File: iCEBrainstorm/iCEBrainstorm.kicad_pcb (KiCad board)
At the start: 2 copper layers, 31 parts, among them J1 Connector, USB-TYPE-C-16P, J2 Conn_01x03_Pin, U1 STM32F103C8T6, U3 ICE40UP5K-SG48ITR, U6 AMS1117, X1 X322516MLB4SI

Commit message: did some things
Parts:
- removed H5: MountingHole_Pad, MountingHole:MountingHole_3.2mm_M3_DIN965_Pad
- removed J2: Conn_01x03_Pin, Connector_PinHeader_2.00mm:PinHeader_1x03_P2.00mm_Vertical
- added C14: 4.7uF, PCM_JLCPCB:C_0805, F.Cu at (67.9, 43.2)
- added C15: 100nF, PCM_JLCPCB:C_0603, F.Cu at (71.1, 47.6)
- added C16: 4.7uF, PCM_JLCPCB:C_0805, F.Cu at (63.8, 50.4)
- added C17: 100nF, PCM_JLCPCB:C_0603, F.Cu at (67.9, 49.2)
- added C18: 4.7uF, PCM_JLCPCB:C_0805, F.Cu at (63.8, 53.5)
- added C19: 100nF, PCM_JLCPCB:C_0603, F.Cu at (67.9, 51.5)
- added C20: 22uF, PCM_JLCPCB:C_0805, F.Cu at (86.4, 72.4)
- added C21: 22uF, PCM_JLCPCB:C_0805, F.Cu at (80.0, 77.5)
- added H4: MountingHole_Pad, MountingHole:MountingHole_2.7mm_Pad, F.Cu at (39.3, 66.1)
- added J3: Conn_01x04_Pin, Connector_PinHeader_2.00mm:PinHeader_1x04_P2.00mm_Vertical, F.Cu at (103.3, 91.4)
- added R4: 5.1kΩ, PCM_JLCPCB:R_0603, F.Cu at (206.2, 75.0)
- added R5: 5.1kΩ, PCM_JLCPCB:R_0603, F.Cu at (206.2, 77.3)
- added R6: 15kΩ, PCM_JLCPCB:R_0603, F.Cu at (66.0, 108.0)
- added SW1: SW_DIP_x08, Button_Switch_THT:SW_DIP_SPSTx08_Slide_6.7x21.88mm_W7.62mm_P2.54mm_LowProfile, F.Cu at (115.6, 64.8)
- added SW2: SW_DIP_x08, Button_Switch_THT:SW_DIP_SPSTx08_Slide_6.7x21.88mm_W7.62mm_P2.54mm_LowProfile, F.Cu at (143.5, 108.0)
- added U2: STM32F412RETx, Package_QFP:LQFP-64_10x10mm_P0.5mm, F.Cu at (99.1, 64.8)
- R1: value 10kΩ -> 15kΩ
- U1: value STM32F103C8T6 -> AMS1117-1.2; footprint PCM_JLCPCB:LQFP-48_7x7mm_P0.5mm -> PCM_JLCPCB:SOT-223-3_L6.5-W3.4-P2.30-LS7.0-BR
- U6: value AMS1117 -> AMS1117-3.3
- X1: value X322516MLB4SI -> 16 MHz
- moved H1 104.0 mm to (39.4, 45.7)
- moved H2 104.0 mm to (39.4, 52.7)
- moved H3 104.0 mm to (39.4, 59.6)
- moved C11 83.0 mm to (80.0, 61.0), turned to 180 degrees
- moved C10 79.7 mm to (86.4, 54.6), turned to 90 degrees
- moved U6 76.9 mm to (80.0, 54.6)
- moved C6 66.7 mm to (170.2, 80.0)
- moved FB1 66.7 mm to (165.7, 79.9)
- moved C1 66.7 mm to (161.5, 59.0)
- moved C2 66.7 mm to (161.5, 61.2)
- moved C3 66.7 mm to (161.5, 63.5)
- moved C4 66.7 mm to (161.5, 65.7)
- moved C5 66.7 mm to (161.5, 68.0)
- moved C7 66.7 mm to (161.5, 70.2)
- moved C8 66.7 mm to (161.5, 72.5)
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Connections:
- C12 pad 1: unconnected-(C12-Pad1) -> GND
- C12 pad 2: unconnected-(C12-Pad2) -> /RCC_OSC_IN
- C13 pad 1: unconnected-(C13-Pad1) -> /RCC_OSC_OUT
- C13 pad 2: unconnected-(C13-Pad2) -> GND
- J1 pad A12B1: Net-(J1-GND-PadA12B1) -> GND
- J1 pad A5: unconnected-(J1-CC1-PadA5) -> Net-(J1-CC1)
- J1 pad A6: unconnected-(J1-D+-PadA6) -> /USB_D+
- J1 pad A7: unconnected-(J1-D--PadA7) -> /USB_D-
- J1 pad A9B4: Net-(J1-VBUS-PadA9B4) -> VBUS
- J1 pad B12A1: Net-(J1-GND-PadA12B1) -> GND
- J1 pad B5: unconnected-(J1-CC2-PadB5) -> Net-(J1-CC2)
- J1 pad B6: unconnected-(J1-D+-PadB6) -> /USB_D+
- J1 pad B7: unconnected-(J1-D--PadB7) -> /USB_D-
- J1 pad B9A4: Net-(J1-VBUS-PadA9B4) -> VBUS
- J1 pad S1: unconnected-(J1-SHIELD-PadS1) -> GND
- R1 pad 1: Net-(J2-Pin_2) -> /BOOT0
- R1 pad 2: Net-(U1-BOOT0) -> GND
- U1 pad 1: +3V3 -> GND
- U1 pad 2: unconnected-(U1-PC13-Pad2) -> +1V2
- U1 pad 3: unconnected-(U1-PC14-Pad3) -> VBUS
- U1 pad 4: unconnected-(U1-PC15-Pad4) -> +1V2
- U3 pad 1: unconnected-(U3C-VCCIO_2-Pad1) -> +3V3
- U3 pad 22: unconnected-(U3B-SPI_VCCIO1-Pad22) -> +3V3
- U3 pad 24: unconnected-(U3D-VPP_2V5-Pad24) -> +3V3
- U3 pad 25: unconnected-(U3A-IOT_36b-Pad25) -> Net-(U2-PA0)
- U3 pad 29: unconnected-(U3D-VCCPLL-Pad29) -> /VCCPLL
- U3 pad 30: Net-(U3D-VCC-Pad30) -> +1V2
- U3 pad 33: unconnected-(U3A-VCCIO_0-Pad33) -> +3V3
- U3 pad 49: unconnected-(U3D-GND-Pad49) -> GND
- U3 pad 5: Net-(U3D-VCC-Pad30) -> +1V2
- X1 pad 1: /XPLUS -> /RCC_OSC_IN
- X1 pad 3: /XMIN -> /RCC_OSC_OUT

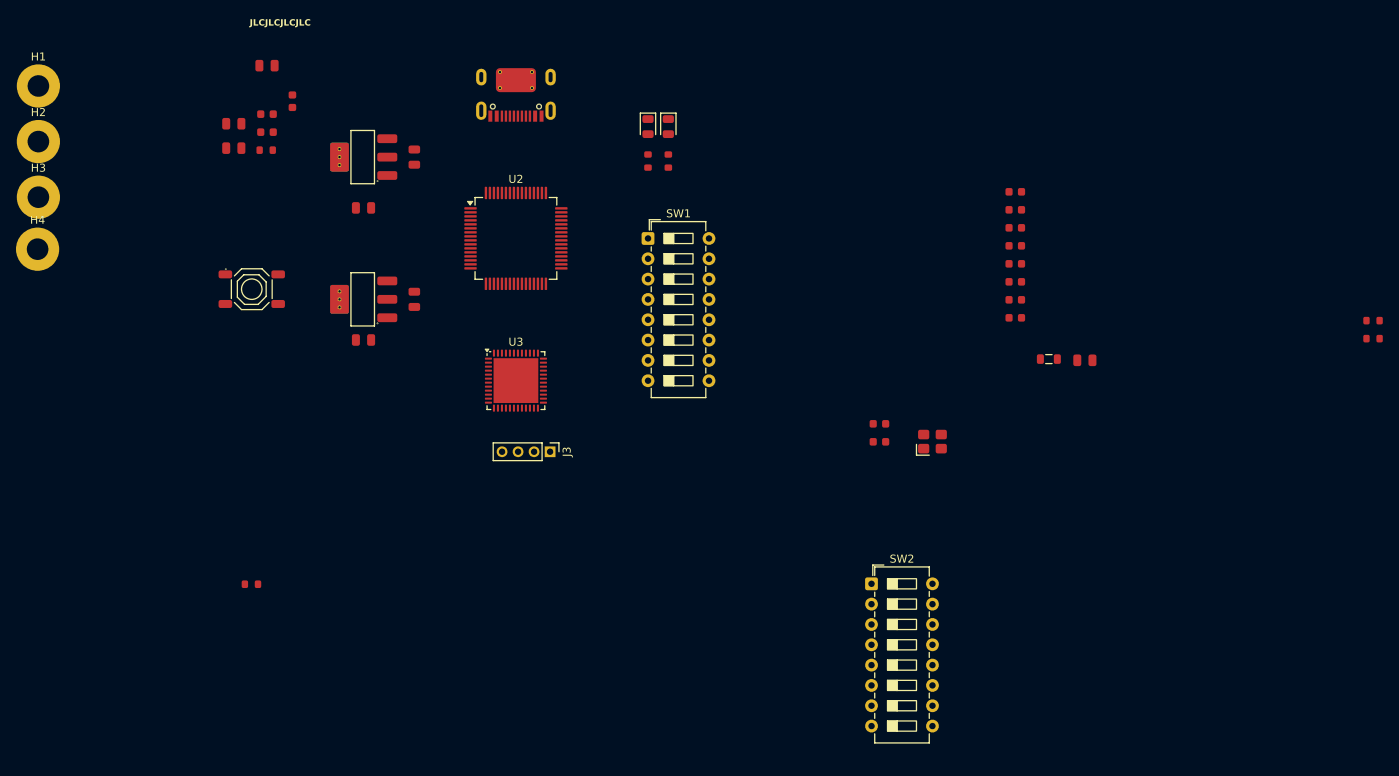
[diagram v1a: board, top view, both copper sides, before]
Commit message: schema und pcb gmacht, quote kostet jetzt 120$ / 10 pcs
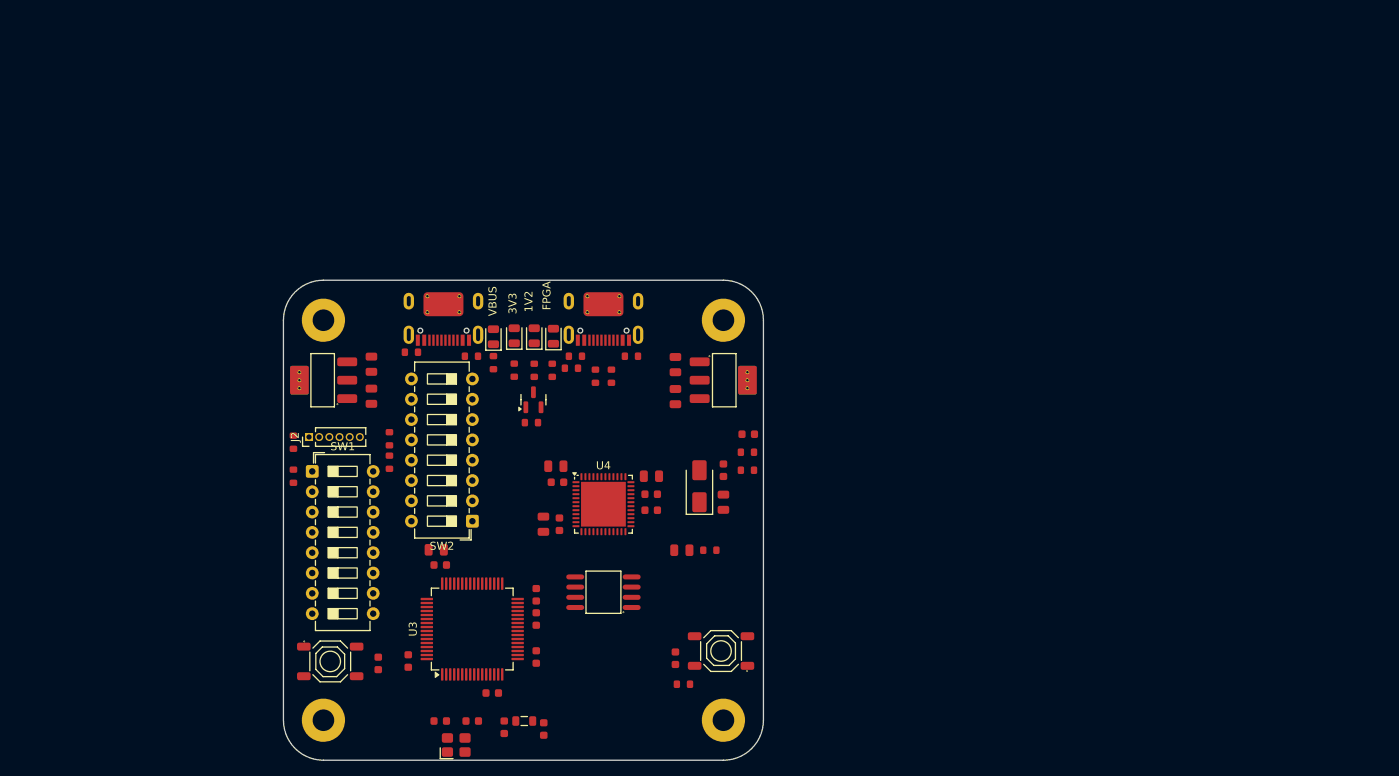
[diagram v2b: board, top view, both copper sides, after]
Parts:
- added C1: 100nF, PCM_JLCPCB:C_0603, F.Cu at (125.0, 93.8)
- added C10: 100nF, PCM_JLCPCB:C_0603, F.Cu at (119.0, 117.2)
- added C17: 100nF, PCM_JLCPCB:C_0603, F.Cu at (101.6, 112.3)
- added C2: 4.7uF, PCM_JLCPCB:C_0805, F.Cu at (125.0, 97.8)
- added C28: 100nF, PCM_JLCPCB:C_0603, F.Cu at (128.1, 89.2)
- added C3: 100nF, PCM_JLCPCB:C_0603, F.Cu at (116.0, 98.8)
- added C6: 4.7uF, PCM_JLCPCB:C_0805, F.Cu at (119.8, 103.8)
- added D1: M4, PCM_JLCPCB:D_SMA, F.Cu at (122.0, 95.8)
- added D2: 1V2 ON - Green, PCM_JLCPCB:D_0805, F.Cu at (101.3, 76.9)
- added D5: Configuration Ready - Green, PCM_JLCPCB:D_0805, F.Cu at (103.8, 77.0)
- added J2: Conn_01x06_Pin, Connector_PinHeader_1.27mm:PinHeader_1x06_P1.27mm_Vertical, F.Cu at (73.2, 89.6)
- added Q1: HL2312, PCM_JLCPCB:Q_SOT-23, F.Cu at (101.2, 84.9)
- added R12: 15kΩ, PCM_JLCPCB:R_0603, F.Cu at (120.0, 120.5)
- added R14: 5.1kΩ, PCM_JLCPCB:R_0603, F.Cu at (113.5, 79.5)
- added R15: 5.1kΩ, PCM_JLCPCB:R_0603, F.Cu at (106.5, 79.5)
- added R16: 1.5kΩ, PCM_JLCPCB:R_0603, F.Cu at (106.0, 81.0)
- added R17: 68Ω, PCM_JLCPCB:R_0603, F.Cu at (109.0, 82.0)
- added R18: 68Ω, PCM_JLCPCB:R_0603, F.Cu at (111.0, 82.0)
- added R19: 15kΩ, PCM_JLCPCB:R_0603, F.Cu at (128.0, 91.5)
- added R20: 15kΩ, PCM_JLCPCB:R_0603, F.Cu at (128.0, 93.8)
- added R21: 2.2kΩ, PCM_JLCPCB:R_0603, F.Cu at (103.6, 81.3)
- added R5: 100Ω, PCM_JLCPCB:R_0603, F.Cu at (123.3, 103.8)
- added R6: 1.5kΩ, PCM_JLCPCB:R_0603, F.Cu at (83.2, 89.8)
- added R7: 1.5kΩ, PCM_JLCPCB:R_0603, F.Cu at (83.2, 92.8)
- added R8: 15kΩ, PCM_JLCPCB:R_0603, F.Cu at (101.0, 87.8)
- added R9: 1.5kΩ, PCM_JLCPCB:R_0603, F.Cu at (101.3, 81.3)
- added S1: RESET, PCM_JLCPCB:SW-SMD_4P-L5.1-W5.1-P3.70-LS6.5-TL-2, F.Cu at (124.7, 116.3)
- added U5: W25Q128, PCM_JLCPCB:SOIC-8_L5.3-W5.3-P1.27-LS8.0-BL, F.Cu at (110.0, 109.0)
- D3: renamed from D1; value POWER ON - Green -> 3V3 ON - Green
- J3: value Conn_01x04_Pin -> Connector, USB-TYPE-C-16P; footprint Connector_PinHeader_2.00mm:PinHeader_1x04_P2.00mm_Vertical -> PCM_JLCPCB:TYPE-C-SMD_HX-TYPE-C-16PIN
- PN1: moved to B.Cu
- moved R4 120.2 mm to (86.0, 79.0), turned to 180 degrees
- moved R3 112.8 mm to (93.5, 79.5)
- moved H2 112.1 mm to (125.0, 125.0)
- moved C11 99.1 mm to (81.8, 117.9), turned to -90 degrees
- moved PN1 91.5 mm to (82.0, 128.5)
- moved C16 90.7 mm to (85.6, 117.6), turned to 90 degrees
- moved H1 86.9 mm to (75.0, 125.0)
- moved H4 86.2 mm to (125.0, 75.0)
- moved C18 84.5 mm to (89.1, 103.7)
- moved C14 83.3 mm to (89.6, 105.6)
- moved C20 83.3 mm to (97.6, 125.9), turned to -90 degrees
- moved C12 81.9 mm to (101.6, 117.1), turned to -90 degrees
- moved C19 81.2 mm to (102.5, 126.1), turned to -90 degrees
- moved C21 80.5 mm to (96.1, 121.6), turned to 180 degrees
- moved FB1 79.7 mm to (100.1, 125.1)
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- renumbered C1 to C11, C2 to C12, C3 to C14, C4 to C15, C5 to C16, C6 to C18, C7 to C19, C8 to C20, C9 to C21, C14 to C22, C15 to C23, C16 to C24, C17 to C25, C18 to C26, C19 to C27, C10 to C4, C20 to C5, C11 to C7, C21 to C8, C12 to C9, D2 to D4, R2 to R10, R3 to R11, R6 to R2, R4 to R3, R5 to R4, S1 to S2, U6 to U1, U1 to U2, U2 to U3, U3 to U4
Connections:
- C13 pad 1: /RCC_OSC_OUT -> /OSC_OUT
- C9 pad 2: /RCC_OSC_IN -> /OSC_IN
- J1 pad A6: /USB_D+ -> /USB_DP
- J1 pad A7: /USB_D- -> /USB_DN
- J1 pad B6: /USB_D+ -> /USB_DP
- J1 pad B7: /USB_D- -> /USB_DN
- SW1 pad 15: +3V3 -> Net-(R7-Pad1)
- SW1 pad 16: +3V3 -> Net-(R6-Pad1)
- U3 pad 14: Net-(U2-PA0) -> unconnected-(U3-PA0-Pad14)
- U3 pad 30: unconnected-(U2-VCAP_1-Pad30) -> Net-(U3-VCAP_1)
- U3 pad 33: unconnected-(U2-PB12-Pad33) -> /SPI2_NSS
- U3 pad 34: unconnected-(U2-PB13-Pad34) -> /SPI2_SCK
- U3 pad 35: unconnected-(U2-PB14-Pad35) -> /SPI2_MISO
- U3 pad 36: unconnected-(U2-PB15-Pad36) -> /SPI2_MOSI
- U3 pad 40: unconnected-(U2-PC9-Pad40) -> /FPGA_CLK
- U3 pad 41: unconnected-(U2-PA8-Pad41) -> /USB_SOF
- U3 pad 42: unconnected-(U2-PA9-Pad42) -> /USB_VBUS
- U3 pad 43: unconnected-(U2-PA10-Pad43) -> /USB_ID
- U3 pad 44: unconnected-(U2-PA11-Pad44) -> /USB_DN
- U3 pad 45: unconnected-(U2-PA12-Pad45) -> /USB_DP
- U3 pad 46: unconnected-(U2-PA13-Pad46) -> /SWDIO
- U3 pad 49: unconnected-(U2-PA14-Pad49) -> /SWCLK
- U3 pad 5: unconnected-(U2-PH0-Pad5) -> /OSC_IN
- U3 pad 55: unconnected-(U2-PB3-Pad55) -> /SWO
- U3 pad 6: unconnected-(U2-PH1-Pad6) -> /OSC_OUT
- U4 pad 10: unconnected-(U3B-IOB_18a-Pad10) -> /SPI2_SCK
- U4 pad 11: unconnected-(U3B-IOB_20a-Pad11) -> /SPI2_NSS
- U4 pad 12: unconnected-(U3B-IOB_22a-Pad12) -> Net-(U4B-IOB_22a)
- U4 pad 13: unconnected-(U3B-IOB_24a-Pad13) -> Net-(U4B-IOB_24a)
- U4 pad 14: unconnected-(U3B-IOB_32a_SPI_SO-Pad14) -> /FPGA_SPI_SO
- U4 pad 15: unconnected-(U3B-IOB_34a_SPI_SCK-Pad15) -> /FPGA_SPI_SCK
- U4 pad 16: unconnected-(U3B-IOB_35b_SPI_SS-Pad16) -> /FPGA_SPI_CS
- U4 pad 17: unconnected-(U3B-IOB_33b_SPI_SI-Pad17) -> /FPGA_SPI_SI
- U4 pad 20: unconnected-(U3B-IOB_25b_G3-Pad20) -> /FPGA_CLK
- U4 pad 21: unconnected-(U3B-IOB_23b-Pad21) -> Net-(U4B-IOB_23b)
- U4 pad 24: +3V3 -> +2V5
- U4 pad 25: Net-(U2-PA0) -> unconnected-(U4A-IOT_36b-Pad25)
- U4 pad 6: unconnected-(U3B-IOB_13b-Pad6) -> /SPI2_MOSI
- U4 pad 7: unconnected-(U3B-CDONE-Pad7) -> Net-(U4B-CDONE)
- U4 pad 8: unconnected-(U3B-~{CRESET}-Pad8) -> /FPGA_NRST
- U4 pad 9: unconnected-(U3B-IOB_16a-Pad9) -> /SPI2_MISO
- X1 pad 1: /RCC_OSC_IN -> /OSC_IN
- X1 pad 3: /RCC_OSC_OUT -> /OSC_OUT
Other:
- board outline added: 60 x 60 mm
- board text added: "1V2"
- board text added: "3V3"
- board text added: "FPGA"
- board text added: "VBUS"

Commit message: pascuu design review
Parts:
- added J5: Conn_01x06_Pin, Connector_PinHeader_1.27mm:PinHeader_1x06_P1.27mm_Vertical, F.Cu at (113.8, 93.0)
- added R13: 1.5kΩ, PCM_JLCPCB:R_0603, F.Cu at (84.0, 99.0)
- added R22: 15kΩ, PCM_JLCPCB:R_0603, F.Cu at (71.5, 98.3)
- added R23: 15kΩ, PCM_JLCPCB:R_0603, F.Cu at (1.32, 0.62)
- moved C26 72.9 mm to (122.8, 163.7), turned to 0 degrees
- moved SW2 69.9 mm to (162.3, 112.9)
- moved C27 68.9 mm to (122.7, 161.7), turned to 0 degrees
- moved C22 68.1 mm to (110.9, 162.4), turned to 180 degrees
- moved C23 63.6 mm to (110.9, 160.2), turned to 180 degrees
- moved U4 61.3 mm to (116.9, 158.9), turned to 180 degrees
- moved C24 60.0 mm to (124.4, 156.4), turned to 90 degrees
- moved C3 59.6 mm to (110.9, 158.2), turned to 180 degrees
- moved C25 58.7 mm to (122.4, 156.4), turned to 90 degrees
- moved C15 52.8 mm to (97.8, 162.0), turned to 180 degrees
- moved C17 50.1 mm to (94.8, 162.0), turned to 0 degrees
- moved C12 46.4 mm to (90.0, 162.0), turned to 180 degrees
- moved C18 45.9 mm to (103.4, 147.3), turned to -90 degrees
- moved C14 43.9 mm to (101.5, 147.8), turned to -90 degrees
- moved C19 42.7 mm to (81.0, 162.9), turned to 180 degrees
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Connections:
- net /FPGA_USB_DN renamed /FPGA_USB_D-
- net /FPGA_USB_DP renamed /FPGA_USB_D+
- net /USB_DN renamed /USB_D-
- net /USB_DP renamed /USB_D+
- R2 pad 1: /BOOT1 -> GND
- R2 pad 2: GND -> /BOOT1
- SW1 pad 13: unconnected-(SW1-Pad13) -> Net-(R23-Pad1)
- SW1 pad 14: unconnected-(SW1-Pad14) -> Net-(R13-Pad1)
- SW1 pad 3: unconnected-(SW1-Pad3) -> /FPGA_BOOT
- SW1 pad 4: unconnected-(SW1-Pad4) -> /FPGA_SPI_CS
- U3 pad 20: unconnected-(U3-PA4-Pad20) -> /FPGA_SPI_CS
- U3 pad 21: unconnected-(U3-PA5-Pad21) -> /FPGA_SPI_SCK
- U3 pad 22: unconnected-(U3-PA6-Pad22) -> /FPGA_SPI_SO
- U3 pad 23: unconnected-(U3-PA7-Pad23) -> /FPGA_SPI_SI
- U3 pad 29: unconnected-(U3-PB10-Pad29) -> /FPGA_GLOBAL_0
- U4 pad 10: /SPI2_SCK -> unconnected-(U4B-IOB_18a-Pad10)
- U4 pad 11: /SPI2_NSS -> unconnected-(U4B-IOB_20a-Pad11)
- U4 pad 28: unconnected-(U4A-IOT_41a-Pad28) -> /SPI2_MOSI
- U4 pad 31: unconnected-(U4A-IOT_42b-Pad31) -> /SPI2_MISO
- U4 pad 32: unconnected-(U4A-IOT_43a-Pad32) -> /SPI2_SCK
- U4 pad 34: unconnected-(U4A-IOT_44b-Pad34) -> /SPI2_NSS
- U4 pad 35: unconnected-(U4A-IOT_46b_G0-Pad35) -> /FPGA_GLOBAL_0
- U4 pad 37: unconnected-(U4A-IOT_45a_G1-Pad37) -> /FPGA_GLOBAL_1
- U4 pad 44: unconnected-(U4C-IOB_3b_G6-Pad44) -> /FPGA_GLOBAL_6
- U4 pad 6: /SPI2_MOSI -> unconnected-(U4B-IOB_13b-Pad6)
- U4 pad 9: /SPI2_MISO -> /FPGA_BOOT

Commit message: finalised the schematic
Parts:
- added C29: 1uF, PCM_JLCPCB:C_0603, F.Cu at (191.0, 161.1)
- added C30: 1uF, PCM_JLCPCB:C_0603, F.Cu at (191.0, 153.0)
- added C31: 1uF, PCM_JLCPCB:C_0603, F.Cu at (204.8, 152.9)
- added C32: 1uF, PCM_JLCPCB:C_0603, F.Cu at (205.6, 161.6)
- added D10: Green, PCM_JLCPCB:D_0805, F.Cu at (179.5, 98.4)
- added D11: Green, PCM_JLCPCB:D_0805, F.Cu at (179.5, 95.4)
- added D12: Green, PCM_JLCPCB:D_0805, F.Cu at (179.5, 92.3)
- added D13: Green, PCM_JLCPCB:D_0805, F.Cu at (179.6, 116.8)
- added D6: Green, PCM_JLCPCB:D_0805, F.Cu at (179.5, 110.7)
- added D7: Green, PCM_JLCPCB:D_0805, F.Cu at (179.5, 107.6)
- added D8: Green, PCM_JLCPCB:D_0805, F.Cu at (179.5, 104.6)
- added D9: Green, PCM_JLCPCB:D_0805, F.Cu at (179.5, 101.5)
- added J10: Conn_01x02_Pin, Connector_PinHeader_1.27mm:PinHeader_1x02_P1.27mm_Vertical, F.Cu at (118.7, 176.5)
- added J4: Conn_01x16_Pin, Connector_PinHeader_1.27mm:PinHeader_1x16_P1.27mm_Vertical, F.Cu at (70.8, 160.6)
- added J6: Conn_01x02_Pin, Connector_PinHeader_1.27mm:PinHeader_1x02_P1.27mm_Vertical, F.Cu at (100.5, 179.2)
- added J7: Conn_01x03_Pin, Connector_PinHeader_1.27mm:PinHeader_1x03_P1.27mm_Vertical, F.Cu at (93.0, 174.2)
- added J8: Conn_01x03_Pin, Connector_PinHeader_1.27mm:PinHeader_1x03_P1.27mm_Vertical, F.Cu at (112.0, 176.5)
- added J9: Conn_01x02_Pin, Connector_PinHeader_1.27mm:PinHeader_1x02_P1.27mm_Vertical, F.Cu at (70.5, 166.5)
- added JP1: SolderJumper_2_Bridged, Jumper:SolderJumper-2_P1.3mm_Bridged_RoundedPad1.0x1.5mm, F.Cu at (130.5, 143.6)
- added JP2: SolderJumper_2_Bridged, Jumper:SolderJumper-2_P1.3mm_Bridged_RoundedPad1.0x1.5mm, F.Cu at (122.5, 146.9)
- added JP3: SolderJumper_2_Bridged, Jumper:SolderJumper-2_P1.3mm_Bridged_RoundedPad1.0x1.5mm, F.Cu at (119.8, 146.9)
- added JP4: SolderJumper_2_Bridged, Jumper:SolderJumper-2_P1.3mm_Bridged_RoundedPad1.0x1.5mm, F.Cu at (116.9, 146.9)
- added JP5: SolderJumper_2_Bridged, Jumper:SolderJumper-2_P1.3mm_Bridged_RoundedPad1.0x1.5mm, F.Cu at (114.0, 146.9)
- added JP6: SolderJumper_2_Open, Jumper:SolderJumper-2_P1.3mm_Open_RoundedPad1.0x1.5mm, F.Cu at (89.0, 167.7)
- added JP7: SolderJumper_2_Open, Jumper:SolderJumper-2_P1.3mm_Open_RoundedPad1.0x1.5mm, F.Cu at (92.0, 167.7)
- added JP8: SolderJumper_2_Open, Jumper:SolderJumper-2_P1.3mm_Open_RoundedPad1.0x1.5mm, F.Cu at (95.0, 167.7)
- added JP9: SolderJumper_2_Open, Jumper:SolderJumper-2_P1.3mm_Open_RoundedPad1.0x1.5mm, F.Cu at (98.0, 167.7)
- added R24: 15kΩ, PCM_JLCPCB:R_0603, F.Cu at (166.5, 112.5)
- added R25: 15kΩ, PCM_JLCPCB:R_0603, F.Cu at (166.5, 110.0)
- added R26: 15kΩ, PCM_JLCPCB:R_0603, F.Cu at (166.0, 107.5)
- added R27: 15kΩ, PCM_JLCPCB:R_0603, F.Cu at (166.0, 105.0)
- added R28: 15kΩ, PCM_JLCPCB:R_0603, F.Cu at (165.5, 102.5)
- added R29: 15kΩ, PCM_JLCPCB:R_0603, F.Cu at (166.0, 100.0)
- added R30: 15kΩ, PCM_JLCPCB:R_0603, F.Cu at (165.7, 97.5)
- added R31: 15kΩ, PCM_JLCPCB:R_0603, F.Cu at (166.0, 95.0)
- added R32: 1.5kΩ, PCM_JLCPCB:R_0603, F.Cu at (183.3, 113.9)
- added R33: 1.5kΩ, PCM_JLCPCB:R_0603, F.Cu at (183.2, 110.9)
- added R34: 1.5kΩ, PCM_JLCPCB:R_0603, F.Cu at (183.2, 107.9)
- added R35: 1.5kΩ, PCM_JLCPCB:R_0603, F.Cu at (183.2, 104.4)
- added R36: 1.5kΩ, PCM_JLCPCB:R_0603, F.Cu at (183.2, 101.4)
- added R37: 1.5kΩ, PCM_JLCPCB:R_0603, F.Cu at (183.3, 98.4)
- added R38: 1.5kΩ, PCM_JLCPCB:R_0603, F.Cu at (183.2, 95.4)
- added R39: 1.5kΩ, PCM_JLCPCB:R_0603, F.Cu at (183.3, 92.4)
- added R40: 1.5kΩ, PCM_JLCPCB:R_0603, F.Cu at (183.2, 116.8)
- added R56: 15kΩ, PCM_JLCPCB:R_0603, F.Cu at (190.8, 162.8)
- added R57: 1.5kΩ, PCM_JLCPCB:R_0603, F.Cu at (190.8, 159.1)
- added R58: 15kΩ, PCM_JLCPCB:R_0603, F.Cu at (191.0, 154.8)
- added R59: 1.5kΩ, PCM_JLCPCB:R_0603, F.Cu at (191.0, 151.2)
- added R60: 15kΩ, PCM_JLCPCB:R_0603, F.Cu at (204.8, 154.9)
- added R61: 1.5kΩ, PCM_JLCPCB:R_0603, F.Cu at (204.8, 150.9)
- added R62: 15kΩ, PCM_JLCPCB:R_0603, F.Cu at (205.6, 163.3)
- added R63: 1.5kΩ, PCM_JLCPCB:R_0603, F.Cu at (205.6, 159.8)
- added S3: RESET, PCM_JLCPCB:SW-SMD_4P-L5.1-W5.1-P3.70-LS6.5-TL-2, F.Cu at (184.5, 161.0)
- added S4: RESET, PCM_JLCPCB:SW-SMD_4P-L5.1-W5.1-P3.70-LS6.5-TL-2, F.Cu at (184.7, 153.1)
- added S5: RESET, PCM_JLCPCB:SW-SMD_4P-L5.1-W5.1-P3.70-LS6.5-TL-2, F.Cu at (198.8, 153.0)
- added S6: RESET, PCM_JLCPCB:SW-SMD_4P-L5.1-W5.1-P3.70-LS6.5-TL-2, F.Cu at (199.6, 161.6)
- D1: value M4 -> Green; footprint PCM_JLCPCB:D_SMA -> PCM_JLCPCB:D_0805
- R23: value 15kΩ -> 1.5kΩ
- moved R23 99.0 mm to (36.2, 93.2)
- moved D1 60.3 mm to (179.5, 113.8), turned to 180 degrees
- moved J2 55.0 mm to (94.8, 140.0), turned to -90 degrees
- moved R22 50.0 mm to (22.1, 90.9), turned to 0 degrees
- moved R2 49.1 mm to (22.9, 87.4), turned to 0 degrees
- moved R1 48.9 mm to (22.6, 85.2), turned to 180 degrees
- moved SW1 48.9 mm to (25.5, 85.3)
- moved R13 48.5 mm to (36.2, 90.4)
- moved R7 47.9 mm to (35.6, 87.7), turned to 0 degrees
- moved R6 47.6 mm to (35.9, 85.2), turned to 0 degrees
- moved R12 41.2 mm to (130.9, 160.2)
- moved R20 32.0 mm to (96.5, 99.2), turned to 90 degrees
- moved C28 31.8 mm to (99.0, 102.0)
- moved C5 27.1 mm to (146.0, 82.5)
- moved C8 27.1 mm to (146.0, 78.5)
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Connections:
- net Net-(U4B-IOB_23b) renamed /FUD+
- net Net-(U4B-IOB_24a) renamed /FUD-
- C1 pad 1: +3V3 -> +2V5
- D1 pad 1: +2V5 -> Net-(D1-Pad1)
- D1 pad 2: +3V3 -> /OUT0
- J2 pad 4: /SWDO -> /SWO
- R16 pad 2: /FPGA_USB_D- -> /FPGA_USB_D+
- R17 pad 1: /FPGA_USB_D- -> /FPGA_USB_D+
- R18 pad 1: /FPGA_USB_D+ -> /FPGA_USB_D-
- SW2 pad 1: unconnected-(SW2-Pad1) -> /IN0
- SW2 pad 10: unconnected-(SW2-Pad10) -> +3V3
- SW2 pad 11: unconnected-(SW2-Pad11) -> +3V3
- SW2 pad 12: unconnected-(SW2-Pad12) -> +3V3
- SW2 pad 13: unconnected-(SW2-Pad13) -> +3V3
- SW2 pad 14: unconnected-(SW2-Pad14) -> +3V3
- SW2 pad 15: unconnected-(SW2-Pad15) -> +3V3
- SW2 pad 16: unconnected-(SW2-Pad16) -> +3V3
- SW2 pad 2: unconnected-(SW2-Pad2) -> /IN1
- SW2 pad 3: unconnected-(SW2-Pad3) -> /IN2
- SW2 pad 4: unconnected-(SW2-Pad4) -> /IN3
- SW2 pad 5: unconnected-(SW2-Pad5) -> /IN4
- SW2 pad 6: unconnected-(SW2-Pad6) -> /IN5
- SW2 pad 7: unconnected-(SW2-Pad7) -> /IN6
- SW2 pad 8: unconnected-(SW2-Pad8) -> /IN7
- SW2 pad 9: unconnected-(SW2-Pad9) -> +3V3
- U3 pad 10: unconnected-(U3-PC2-Pad10) -> /PC2
- U3 pad 11: unconnected-(U3-PC3-Pad11) -> /PC3
- U3 pad 14: unconnected-(U3-PA0-Pad14) -> /IN0
- U3 pad 15: unconnected-(U3-PA1-Pad15) -> /IN1
- U3 pad 16: unconnected-(U3-PA2-Pad16) -> /USART2_TX
- U3 pad 17: unconnected-(U3-PA3-Pad17) -> /USART2_RX
- U3 pad 2: unconnected-(U3-PC13-Pad2) -> /PC13
- U3 pad 20: /FPGA_SPI_CS -> Net-(JP6-A)
- U3 pad 21: /FPGA_SPI_SCK -> /SPI1_SCK
- U3 pad 22: /FPGA_SPI_SO -> /SPI1_MISO
- U3 pad 23: /FPGA_SPI_SI -> /SPI1_MOSI
- U3 pad 24: unconnected-(U3-PC4-Pad24) -> /PC4
- U3 pad 25: unconnected-(U3-PC5-Pad25) -> /PC5
- U3 pad 26: unconnected-(U3-PB0-Pad26) -> /I2S5_CK
- U3 pad 27: unconnected-(U3-PB1-Pad27) -> /I2S5_WS
- U3 pad 29: /FPGA_GLOBAL_0 -> /FPGA_CLK
- U3 pad 3: unconnected-(U3-PC14-Pad3) -> /PC14
- U3 pad 37: unconnected-(U3-PC6-Pad37) -> /PC6
- U3 pad 38: unconnected-(U3-PC7-Pad38) -> /PC7
- U3 pad 39: unconnected-(U3-PC8-Pad39) -> /PC8
- U3 pad 4: unconnected-(U3-PC15-Pad4) -> /PC15
- U3 pad 41: /USB_SOF -> /FPGA_GLOBAL_1
- U3 pad 42: /USB_VBUS -> /USART1_TX
- U3 pad 43: /USB_ID -> /USART1_RX
- U3 pad 50: unconnected-(U3-PA15-Pad50) -> /FPGA_BUS0
- U3 pad 51: unconnected-(U3-PC10-Pad51) -> /PC10
- U3 pad 52: unconnected-(U3-PC11-Pad52) -> /PC11
- U3 pad 53: unconnected-(U3-PC12-Pad53) -> /PC12
- U3 pad 54: unconnected-(U3-PD2-Pad54) -> /FPGA_BUS1
- U3 pad 56: unconnected-(U3-PB4-Pad56) -> /IN3
- U3 pad 57: unconnected-(U3-PB5-Pad57) -> /OUT8
- U3 pad 58: unconnected-(U3-PB6-Pad58) -> /I2C1_SCL
- U3 pad 59: unconnected-(U3-PB7-Pad59) -> /I2C1_SDA
- U3 pad 61: unconnected-(U3-PB8-Pad61) -> /I2S5_SD
- U3 pad 62: unconnected-(U3-PB9-Pad62) -> /BTN0
- U3 pad 8: unconnected-(U3-PC0-Pad8) -> /PC0
- U3 pad 9: unconnected-(U3-PC1-Pad9) -> /PC1
- U4 pad 10: unconnected-(U4B-IOB_18a-Pad10) -> /IN4
- U4 pad 11: unconnected-(U4B-IOB_20a-Pad11) -> /IN5
- U4 pad 14: /FPGA_SPI_SO -> Net-(JP2-B)
- U4 pad 15: /FPGA_SPI_SCK -> Net-(JP4-B)
- U4 pad 16: /FPGA_SPI_CS -> Net-(JP5-B)
- U4 pad 17: /FPGA_SPI_SI -> Net-(JP3-B)
- U4 pad 18: unconnected-(U4B-IOB_31b-Pad18) -> /I2C1_SDA
- U4 pad 19: unconnected-(U4B-IOB_29b-Pad19) -> /I2C1_SCL
- U4 pad 2: unconnected-(U4C-IOB_6a-Pad2) -> /OUT1
- U4 pad 20: /FPGA_CLK -> /FPGA_GLOBAL_3
- U4 pad 23: unconnected-(U4A-IOT_37a-Pad23) -> /FPGA_BUS0
- U4 pad 25: unconnected-(U4A-IOT_36b-Pad25) -> /FPGA_BUS1
- U4 pad 26: unconnected-(U4A-IOT_39a-Pad26) -> /USART1_RX
- U4 pad 27: unconnected-(U4A-IOT_38b-Pad27) -> /USART1_TX
- U4 pad 3: unconnected-(U4C-IOB_9b-Pad3) -> /OUT0
- U4 pad 35: /FPGA_GLOBAL_0 -> /FPGA_CLK
- U4 pad 36: unconnected-(U4A-IOT_48b-Pad36) -> /BTN1
- U4 pad 38: unconnected-(U4A-IOT_50b-Pad38) -> /BTN2
- U4 pad 39: unconnected-(U4A-RGB0-Pad39) -> /RGB0
- U4 pad 4: unconnected-(U4C-IOB_8a-Pad4) -> /IN7
- U4 pad 40: unconnected-(U4A-RGB1-Pad40) -> /RGB1
- U4 pad 41: unconnected-(U4A-RGB2-Pad41) -> /RGB2
- U4 pad 42: unconnected-(U4A-IOT_51a-Pad42) -> /OUT7
- U4 pad 43: unconnected-(U4A-IOT_49a-Pad43) -> /OUT6
- U4 pad 45: unconnected-(U4C-IOB_5b-Pad45) -> /OUT5
- U4 pad 46: unconnected-(U4C-IOB_0a-Pad46) -> /OUT4
- U4 pad 47: unconnected-(U4C-IOB_2a-Pad47) -> /OUT3
- U4 pad 48: unconnected-(U4C-IOB_4a-Pad48) -> /OUT2
- U4 pad 6: unconnected-(U4B-IOB_13b-Pad6) -> /IN6
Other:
- board size 60 x 60 mm -> 70 x 70 mm
